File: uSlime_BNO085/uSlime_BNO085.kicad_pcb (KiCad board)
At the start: 2 copper layers, 16.7 x 12.8 mm, 14 parts, among them CN1 X1502WR-05K-N0SN, U1 BNO085

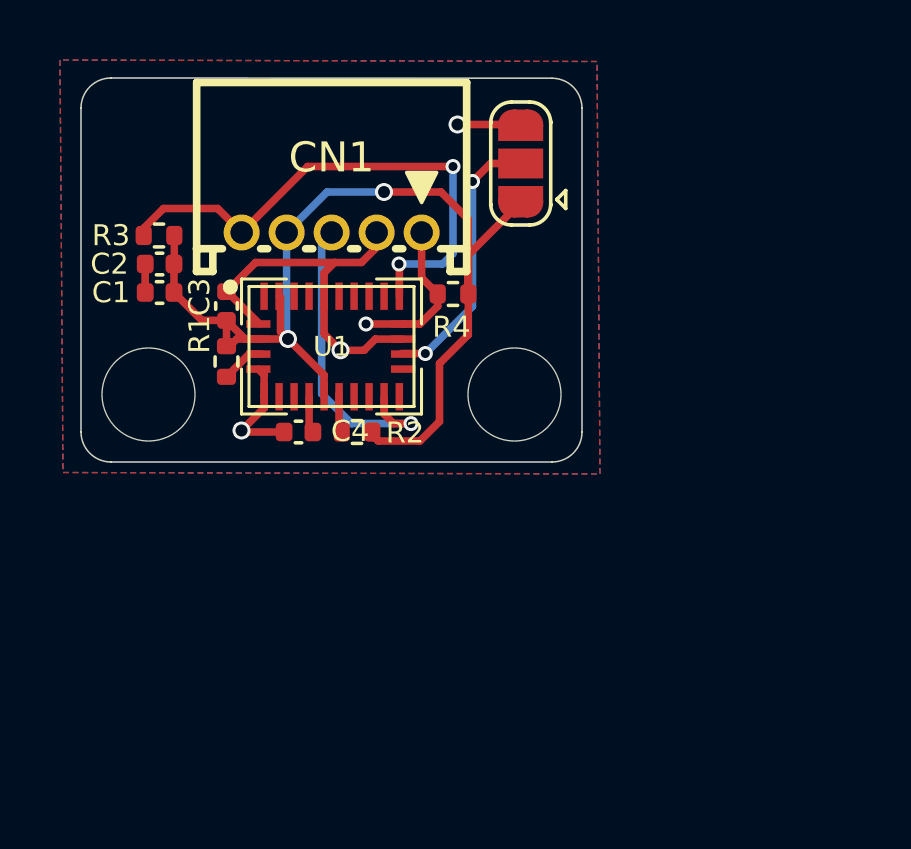
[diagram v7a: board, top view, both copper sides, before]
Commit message: Connect pin 26 to GND
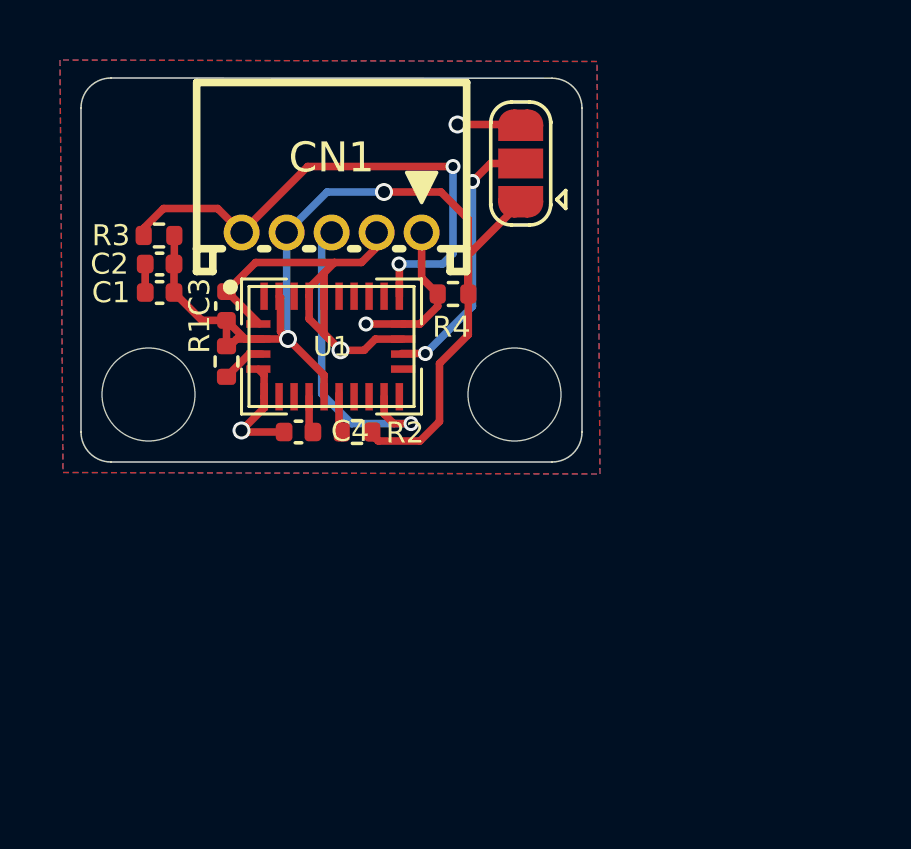
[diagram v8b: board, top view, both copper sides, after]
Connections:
- U1 pad 26: unconnected-(U1-XOUT32/CLKSEL1-Pad26) -> GND
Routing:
- net GND: track 20.2 -> 23.4 mm
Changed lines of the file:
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@@
 	(net 15 "unconnected-(U1-RESV_NC-Pad7)")
 	(net 16 "unconnected-(U1-RESV_NC-Pad12)")
-	(net 17 "unconnected-(U1-XOUT32{slash}CLKSEL1-Pad26)")
-	(net 18 "unconnected-(U1-RESV_NC-Pad23)")
-	(net 19 "unconnected-(U1-RESV_NC-Pad22)")
-	(net 20 "unconnected-(U1-XIN32-Pad27)")
-	(net 21 "unconnected-(U1-ENV_SDA-Pad16)")
-	(net 22 "unconnected-(U1-RESV_NC-Pad8)")
+	(net 17 "unconnected-(U1-RESV_NC-Pad23)")
+	(net 18 "unconnected-(U1-RESV_NC-Pad22)")
+	(net 19 "unconnected-(U1-XIN32-Pad27)")
+	(net 20 "unconnected-(U1-ENV_SDA-Pad16)")
+	(net 21 "unconnected-(U1-RESV_NC-Pad8)")
 	(footprint "Capacitor_SMD:C_0402_1005Metric"
 		(layer "F.Cu")
@@
 			(size 0.25 0.9144)
 			(layers "F.Cu" "F.Paste" "F.Mask")
-			(net 22 "unconnected-(U1-RESV_NC-Pad8)")
+			(net 21 "unconnected-(U1-RESV_NC-Pad8)")
 			(pinfunction "RESV_NC")
 			(pintype "no_connect")
@@
 			(size 0.25 0.8128)
 			(layers "F.Cu" "F.Paste" "F.Mask")
-			(net 21 "unconnected-(U1-ENV_SDA-Pad16)")
+			(net 20 "unconnected-(U1-ENV_SDA-Pad16)")
 			(pinfunction "ENV_SDA")
 			(pintype "bidirectional+no_connect")
@@
 			(size 0.25 0.9144)
 			(layers "F.Cu" "F.Paste" "F.Mask")
-			(net 19 "unconnected-(U1-RESV_NC-Pad22)")
+			(net 18 "unconnected-(U1-RESV_NC-Pad22)")
 			(pinfunction "RESV_NC")
 			(pintype "no_connect")
@@
 			(size 0.25 0.9144)
 			(layers "F.Cu" "F.Paste" "F.Mask")
-			(net 18 "unconnected-(U1-RESV_NC-Pad23)")
+			(net 17 "unconnected-(U1-RESV_NC-Pad23)")
 			(pinfunction "RESV_NC")
 			(pintype "no_connect")
@@
 			(size 0.25 0.9144)
 			(layers "F.Cu" "F.Paste" "F.Mask")
-			(net 17 "unconnected-(U1-XOUT32{slash}CLKSEL1-Pad26)")
+			(net 1 "GND")
 			(pinfunction "XOUT32/CLKSEL1")
-			(pintype "output+no_connect")
+			(pintype "output")
 			(thermal_bridge_angle 45)
 			(teardrops
@@
 			(size 0.25 0.9144)
 			(layers "F.Cu" "F.Paste" "F.Mask")
-			(net 20 "unconnected-(U1-XIN32-Pad27)")
+			(net 19 "unconnected-(U1-XIN32-Pad27)")
 			(pinfunction "XIN32")
 			(pintype "input+no_connect")
@@
 	)
 	(segment
+		(start 108.25328 96.62266)
+		(end 108.25328 96.34672)
+		(width 0.254)
+		(layer "F.Cu")
+		(net 1)
+	)
+	(segment
 		(start 110.505 94.995)
 		(end 110 95.5)
@@
 	)
 	(segment
+		(start 108.25328 96.34672)
+		(end 108.75328 95.84672)
+		(width 0.254)
+		(layer "F.Cu")
+		(net 1)
+	)
+	(segment
 		(start 105.535 96.47)
 		(end 105.5 96.47)
@@
 	)
 	(segment
+		(start 108.25328 97.378476)
+		(end 109.3 98.425196)
+		(width 0.254)
+		(layer "F.Cu")
+		(net 1)
+	)
+	(segment
 		(start 109.3 98.425196)
 		(end 108.75328 97.878476)
@@
 	)
 	(segment
+		(start 108.25328 96.62266)
+		(end 108.25328 97.378476)
+		(width 0.254)
+		(layer "F.Cu")
+		(net 1)
+	)
+	(segment
 		(start 109.3 98.425196)
 		(end 110.090806 98.425196)
@@
 		(name "$teardrop_padvia$")
 		(hatch full 0.1)
+		(priority 30000)
+		(attr
+			(teardrop
+				(type padvia)
+			)
+		)
+		(connect_pads yes
+			(clearance 0)
+		)
+		(min_thickness 0.0254)
+		(filled_areas_thickness no)
+		(fill yes
+			(thermal_gap 0.5)
+			(thermal_bridge_width 0.5)
+			(island_removal_mode 1)
+			(island_area_min 10)
+		)
+		(polygon
+			(pts
+				(xy 108.965539 97.91113) (xy 108.785934 98.090735) (xy 109.022836 98.540001) (xy 109.300707 98.425903)
+				(xy 109.414805 98.148032)
+			)
+		)
+	)
+	(zone
+		(net 1)
+		(net_name "GND")
+		(layer "F.Cu")
+		(name "$teardrop_padvia$")
+		(hatch full 0.1)
 		(priority 30009)
 		(attr
@@
 			)
 		)
-	)
-	(zone
-		(net 6)
-		(net_name "Net-(JP1-C)")
-		(layer "F.Cu")
-		(name "$teardrop_padvia$")
-		(hatch full 0.1)
-		(priority 30031)
-		(attr
-			(teardrop
-				(type padvia)
-			)
-		)
-		(connect_pads yes
-			(clearance 0)
-		)
-		(min_thickness 0.0254)
-		(filled_areas_thickness no)
-		(fill yes
-			(thermal_gap 0.5)
-			(thermal_bridge_width 0.5)
-			(island_removal_mode 1)
-			(island_area_min 10)
-		)
-		(polygon
-			(pts
-				(xy 111.627797 98.407409) (xy 111.627797 98.661409) (xy 112.032126 98.765379) (xy 112.128797 98.534409)
-				(xy 112.032126 98.303439)
-			)
-		)
